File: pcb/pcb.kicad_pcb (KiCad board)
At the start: 2 copper layers, 52.6 x 26.2 mm, 30 parts, among them J1 Conn_01x01, J2 Conn_01x01, J3 Conn_01x01, J4 Conn_02x05_Odd_Even, J5 RJ45_Amphenol_RJMG1BD3B8K1ANR, J6 Conn_01x01, U1 ENC28J60x-SS, Y1 Crystal

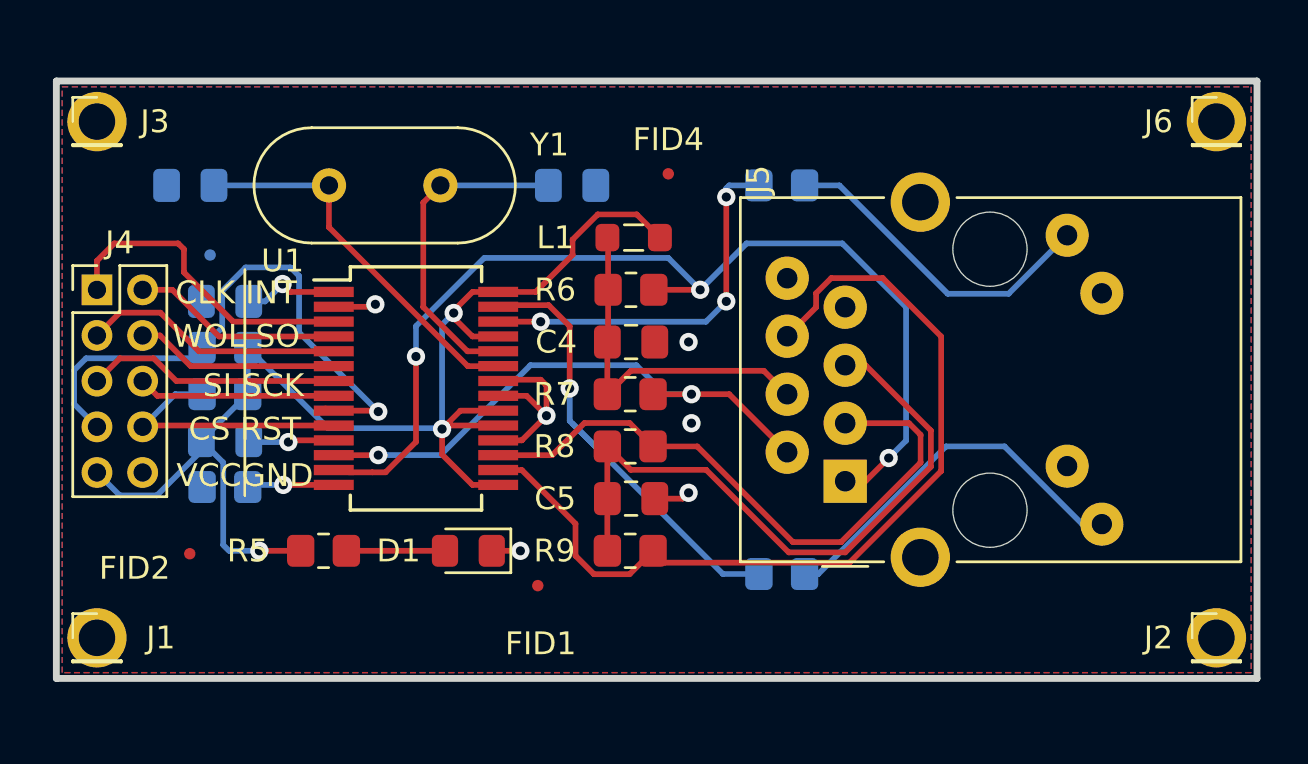
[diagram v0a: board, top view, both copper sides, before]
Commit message: Corrección de pin de montaje
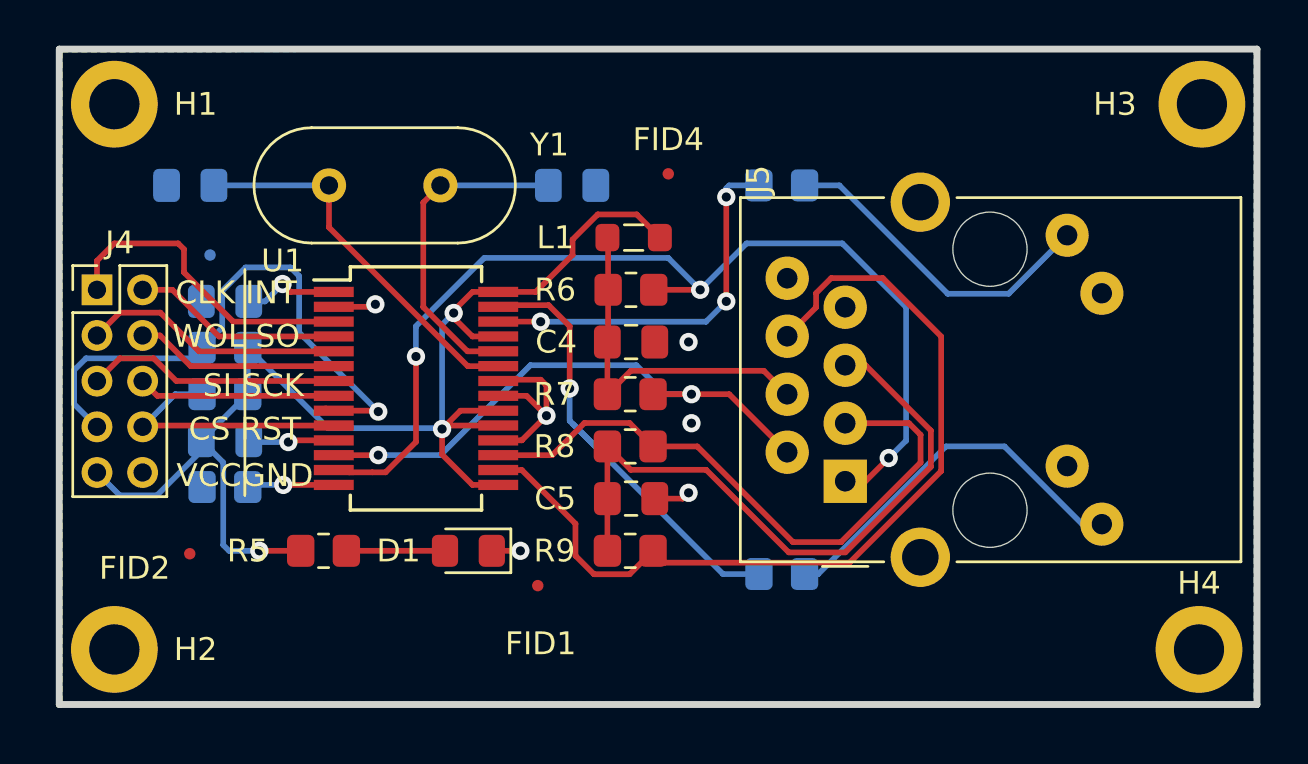
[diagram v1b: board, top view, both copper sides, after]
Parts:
- removed J1, J2, J3, J6: Conn_01x01, Connector_PinHeader_2.00mm:PinHeader_1x01_P2.00mm_Vertical
- added H1: MountingHole, MountingHole:MountingHole_2.2mm_M2_DIN965_Pad, F.Cu at (133.9, 63.2)
- added H2: MountingHole, MountingHole:MountingHole_2.2mm_M2_DIN965_Pad, F.Cu at (133.9, 87.1)
- added H3: MountingHole, MountingHole:MountingHole_2.2mm_M2_DIN965_Pad, F.Cu at (181.5, 63.2)
- added H4: MountingHole, MountingHole:MountingHole_2.2mm_M2_DIN965_Pad, F.Cu at (181.4, 87.1)
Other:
- board size 52.6 x 26.2 mm -> 52.5 x 28.7 mm

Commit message: Correcciones
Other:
- board size 52.5 x 28.7 mm -> 53 x 29 mm
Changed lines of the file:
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@@
-      (effects (font (size 1 1) (thickness 0.15)))
-    )
-    (fp_text user %R (at 0.3 0) (layer F.Fab)
       (effects (font (size 1 1) (thickness 0.15)))
     )
     (fp_circle (center 0 0) (end 1.9 0) (layer Cmts.User) (width 0.15))
     (fp_circle (center 0 0) (end 2.15 0) (layer F.CrtYd) (width 0.05))
+    (fp_text user %R (at 0.3 0) (layer F.Fab)
+      (effects (font (size 1 1) (thickness 0.15)))
+    )
     (pad 1 thru_hole circle (at 0 0) (size 3.8 3.8) (drill 2.2) (layers *.Cu *.Mask))
   )
@@
       (effects (font (size 1 1) (thickness 0.15)))
     )
-    (fp_text user %R (at 0.3 0) (layer F.Fab)
-      (effects (font (size 1 1) (thickness 0.15)))
-    )
     (fp_circle (center 0 0) (end 1.9 0) (layer Cmts.User) (width 0.15))
     (fp_circle (center 0 0) (end 2.15 0) (layer F.CrtYd) (width 0.05))
+    (fp_text user %R (at 0.3 0) (layer F.Fab)
+      (effects (font (size 1 1) (thickness 0.15)))
+    )
     (pad 1 thru_hole circle (at 0 0) (size 3.8 3.8) (drill 2.2) (layers *.Cu *.Mask))
   )
@@
       (effects (font (size 1 1) (thickness 0.15)))
     )
-    (fp_text user %R (at 0.3 0) (layer F.Fab)
-      (effects (font (size 1 1) (thickness 0.15)))
-    )
     (fp_circle (center 0 0) (end 1.9 0) (layer Cmts.User) (width 0.15))
     (fp_circle (center 0 0) (end 2.15 0) (layer F.CrtYd) (width 0.05))
+    (fp_text user %R (at 0.3 0) (layer F.Fab)
+      (effects (font (size 1 1) (thickness 0.15)))
+    )
     (pad 1 thru_hole circle (at 0 0) (size 3.8 3.8) (drill 2.2) (layers *.Cu *.Mask))
   )
@@
       (effects (font (size 1 1) (thickness 0.15)))
     )
-    (fp_text user %R (at 0.3 0) (layer F.Fab)
-      (effects (font (size 1 1) (thickness 0.15)))
-    )
     (fp_circle (center 0 0) (end 1.9 0) (layer Cmts.User) (width 0.15))
     (fp_circle (center 0 0) (end 2.15 0) (layer F.CrtYd) (width 0.05))
+    (fp_text user %R (at 0.3 0) (layer F.Fab)
+      (effects (font (size 1 1) (thickness 0.15)))
+    )
     (pad 1 thru_hole circle (at 0 0) (size 3.8 3.8) (drill 2.2) (layers *.Cu *.Mask))
   )
@@
     (pad R1 thru_hole rect (at 0 0 90) (size 1.9 1.9) (drill 0.9) (layers *.Cu *.Mask)
       (net 20 "Net-(J5-PadR1)"))
-    (model ${KISYS3DMOD}/Connector_RJ.3dshapes/RJ45_Amphenol_RJMG1BD3B8K1ANR.wrl
-      (at (xyz 0 0 0))
-      (scale (xyz 1 1 1))
-      (rotate (xyz 0 0 0))
-    )
-    (model ${KIPRJMOD}/3dshapes/RJMG1BD3B8K1ANR.wrl
-      (at (xyz 0 0 0))
-      (scale (xyz 1 1 1))
-      (rotate (xyz 0 0 0))
-    )
     (model ${KIPRJMOD}/3dshapes/RJMG1BD3B8K1ANR.stp
       (at (xyz 0 0 0))
@@
     (effects (font (size 1 1) (thickness 0.15)))
   )
-  (gr_line (start 183.896 60.833) (end 183.896 89.535) (layer Edge.Cuts) (width 0.3))
-  (gr_line (start 131.445 60.833) (end 183.896 60.833) (layer Edge.Cuts) (width 0.3))
-  (gr_line (start 131.445 89.535) (end 131.445 60.833) (layer Edge.Cuts) (width 0.3))
-  (gr_line (start 131.445 89.535) (end 183.896 89.535) (layer Edge.Cuts) (width 0.3))
+  (gr_line (start 184 61) (end 184 90) (layer Edge.Cuts) (width 0.3))
+  (gr_line (start 131 61) (end 184 61) (layer Edge.Cuts) (width 0.3))
+  (gr_line (start 131 90) (end 131 61) (layer Edge.Cuts) (width 0.3))
+  (gr_line (start 131 90) (end 184 90) (layer Edge.Cuts) (width 0.3))
   (via (at 141.478 78.042) (size 0.8) (drill 0.4) (layers F.Cu B.Cu) (net 1))
   (segment (start 141.553 77.967) (end 141.478 78.042) (width 0.25) (layer F.Cu) (net 1))
@@
     (polygon
       (pts
-        (xy 183.769 89.535) (xy 131.572 89.408) (xy 131.572 60.96) (xy 183.769 60.833)
+        (xy 184 90) (xy 131 90) (xy 131 61) (xy 184 61)
       )
     )
@@
     (polygon
       (pts
-        (xy 183.769 89.408) (xy 131.572 89.408) (xy 131.572 60.96) (xy 183.769 60.833)
+        (xy 184 90) (xy 131 90) (xy 131 61) (xy 184 61)
       )
     )

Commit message: Corrección chica
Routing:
- net Net-(J5-PadR1): vias 3 -> 2
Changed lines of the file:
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@@
     (thickness 1.6)
     (drawings 10)
-    (tracks 234)
+    (tracks 232)
     (zones 0)
     (modules 30)
@@
   (segment (start 157.988 75.946) (end 156.718 74.676) (width 0.25) (layer B.Cu) (net 19))
   (segment (start 159.131 75.946) (end 157.988 75.946) (width 0.25) (layer B.Cu) (net 19))
-  (via (at 167.767 78.74) (size 0.8) (drill 0.4) (layers F.Cu B.Cu) (net 20))
-  (segment (start 166.751 79.756) (end 167.767 78.74) (width 0.25) (layer F.Cu) (net 20))
-  (segment (start 165.862 79.756) (end 166.751 79.756) (width 0.25) (layer F.Cu) (net 20))
-  (segment (start 167.767 78.74) (end 168.529 77.978) (width 0.25) (layer B.Cu) (net 20))
-  (segment (start 168.529 77.978) (end 168.529 72.136) (width 0.25) (layer B.Cu) (net 20))
-  (segment (start 168.529 72.136) (end 165.735 69.342) (width 0.25) (layer B.Cu) (net 20))
   (via (at 159.512 71.374) (size 0.8) (drill 0.4) (layers F.Cu B.Cu) (net 20))
-  (segment (start 161.544 69.342) (end 159.512 71.374) (width 0.25) (layer B.Cu) (net 20))
-  (segment (start 165.735 69.342) (end 161.544 69.342) (width 0.25) (layer B.Cu) (net 20))
   (segment (start 159.512 71.374) (end 157.48 71.374) (width 0.25) (layer F.Cu) (net 20))
   (segment (start 144.136999 79.366999) (end 145.152999 79.366999) (width 0.25) (layer F.Cu) (net 20))
@@
   (segment (start 147.066 72.967998) (end 150.056998 69.977) (width 0.25) (layer B.Cu) (net 20))
   (segment (start 147.066 74.295) (end 147.066 72.967998) (width 0.25) (layer B.Cu) (net 20))
+  (segment (start 168.529 72.136) (end 165.735 69.342) (width 0.25) (layer B.Cu) (net 20))
+  (segment (start 161.544 69.342) (end 159.512 71.374) (width 0.25) (layer B.Cu) (net 20))
+  (segment (start 168.529 77.978) (end 168.529 72.136) (width 0.25) (layer B.Cu) (net 20))
+  (segment (start 166.751 79.756) (end 168.529 77.978) (width 0.25) (layer B.Cu) (net 20))
+  (segment (start 165.735 69.342) (end 161.544 69.342) (width 0.25) (layer B.Cu) (net 20))
+  (segment (start 165.862 79.756) (end 166.751 79.756) (width 0.25) (layer B.Cu) (net 20))
   (segment (start 160.507315 83.82) (end 162.084 83.82) (width 0.25) (layer B.Cu) (net 21))
   (via (at 153.797 75.692) (size 0.8) (drill 0.4) (layers F.Cu B.Cu) (net 21))
@@
   (segment (start 149.334588 74.717) (end 143.256 68.638412) (width 0.25) (layer F.Cu) (net 23))
   (segment (start 150.666 74.717) (end 149.334588 74.717) (width 0.25) (layer F.Cu) (net 23))
-  (segment (start 143.256 66.802) (end 138.219 66.802) (width 0.25) (layer B.Cu) (net 23) (status 1000000))
+  (segment (start 143.256 66.802) (end 138.219 66.802) (width 0.25) (layer B.Cu) (net 23))
   (segment (start 152.865 66.802) (end 148.136 66.802) (width 0.25) (layer B.Cu) (net 24))
   (segment (start 147.386001 67.551999) (end 148.136 66.802) (width 0.25) (layer F.Cu) (net 24))
